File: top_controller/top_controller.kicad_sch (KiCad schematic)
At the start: 119 parts, among them J1 OUT1, J10 USB_C_Receptacle_USB2.0, J11 SWD, J12 UART, J13 BOOT0, J14 BOOT1, J2 OUT2, J3 OUT3, J4 OUT4, J5 OUT5, J6 OUT6, J7 OUT7, J8 OUT8, J9 PIN, SW1 RESET, U1 STM32F103C8Tx, U2 LT3045xMSE, U3 AD5754BREZ, U4 AD5754BREZ, U5 REF192, U6 EPM78V2, U7 REF192, Y1 8MHz

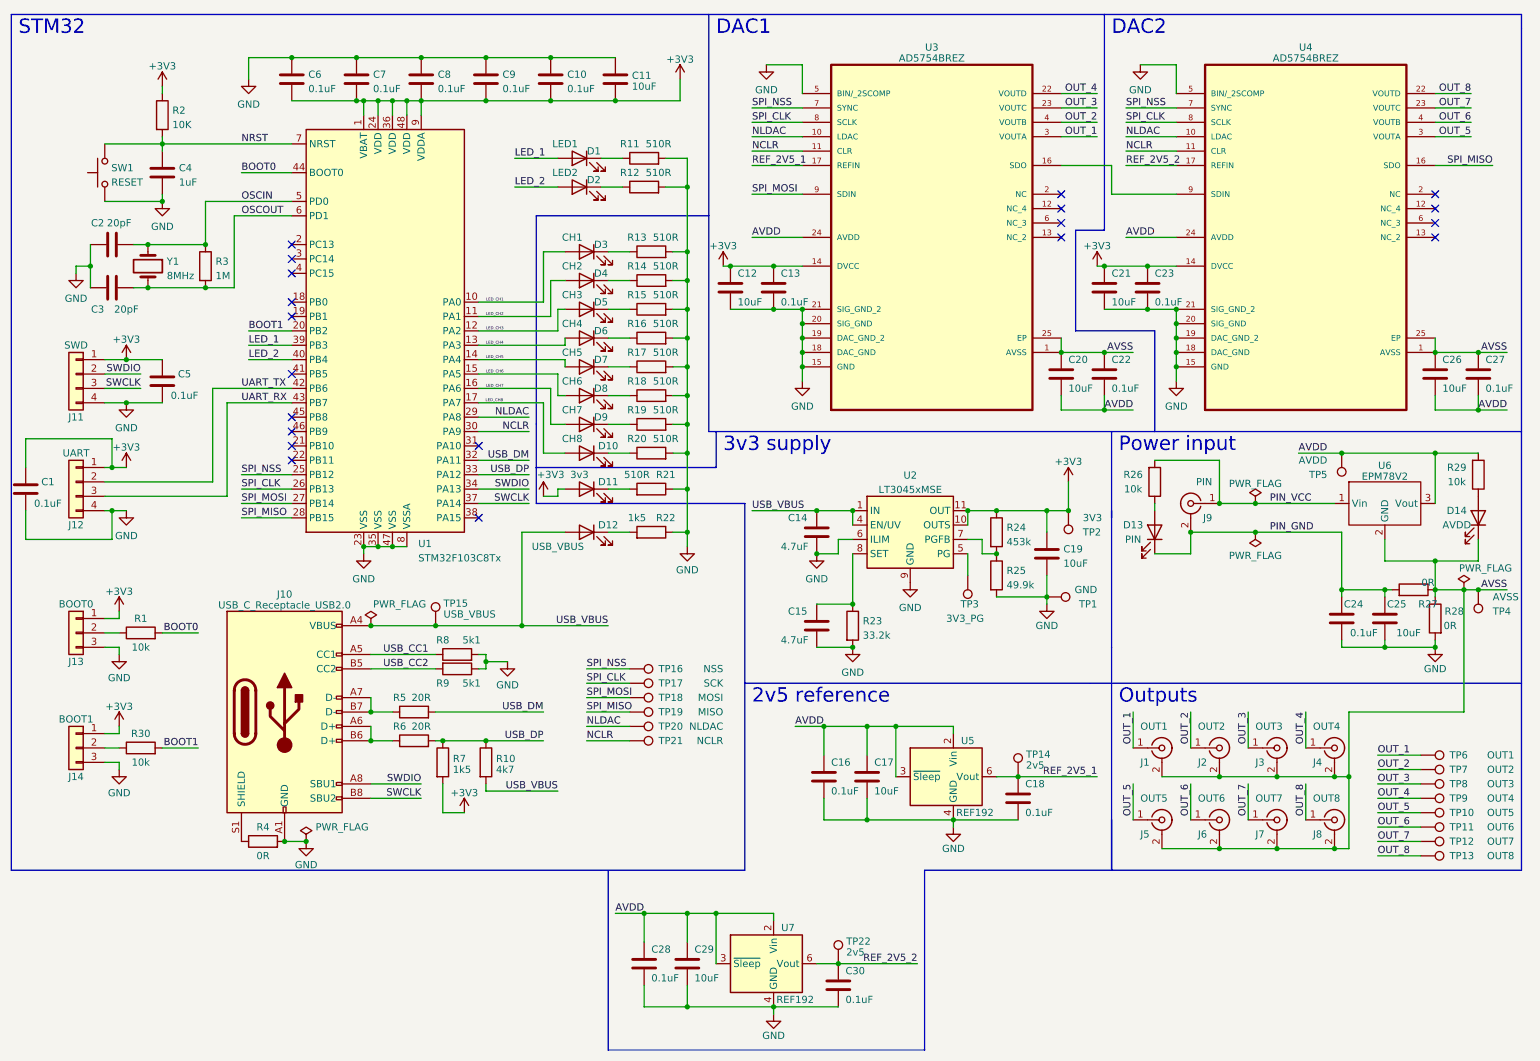
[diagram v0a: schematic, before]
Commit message: GNDA and VDDA redone properly, slightly changed component placement in the schematic
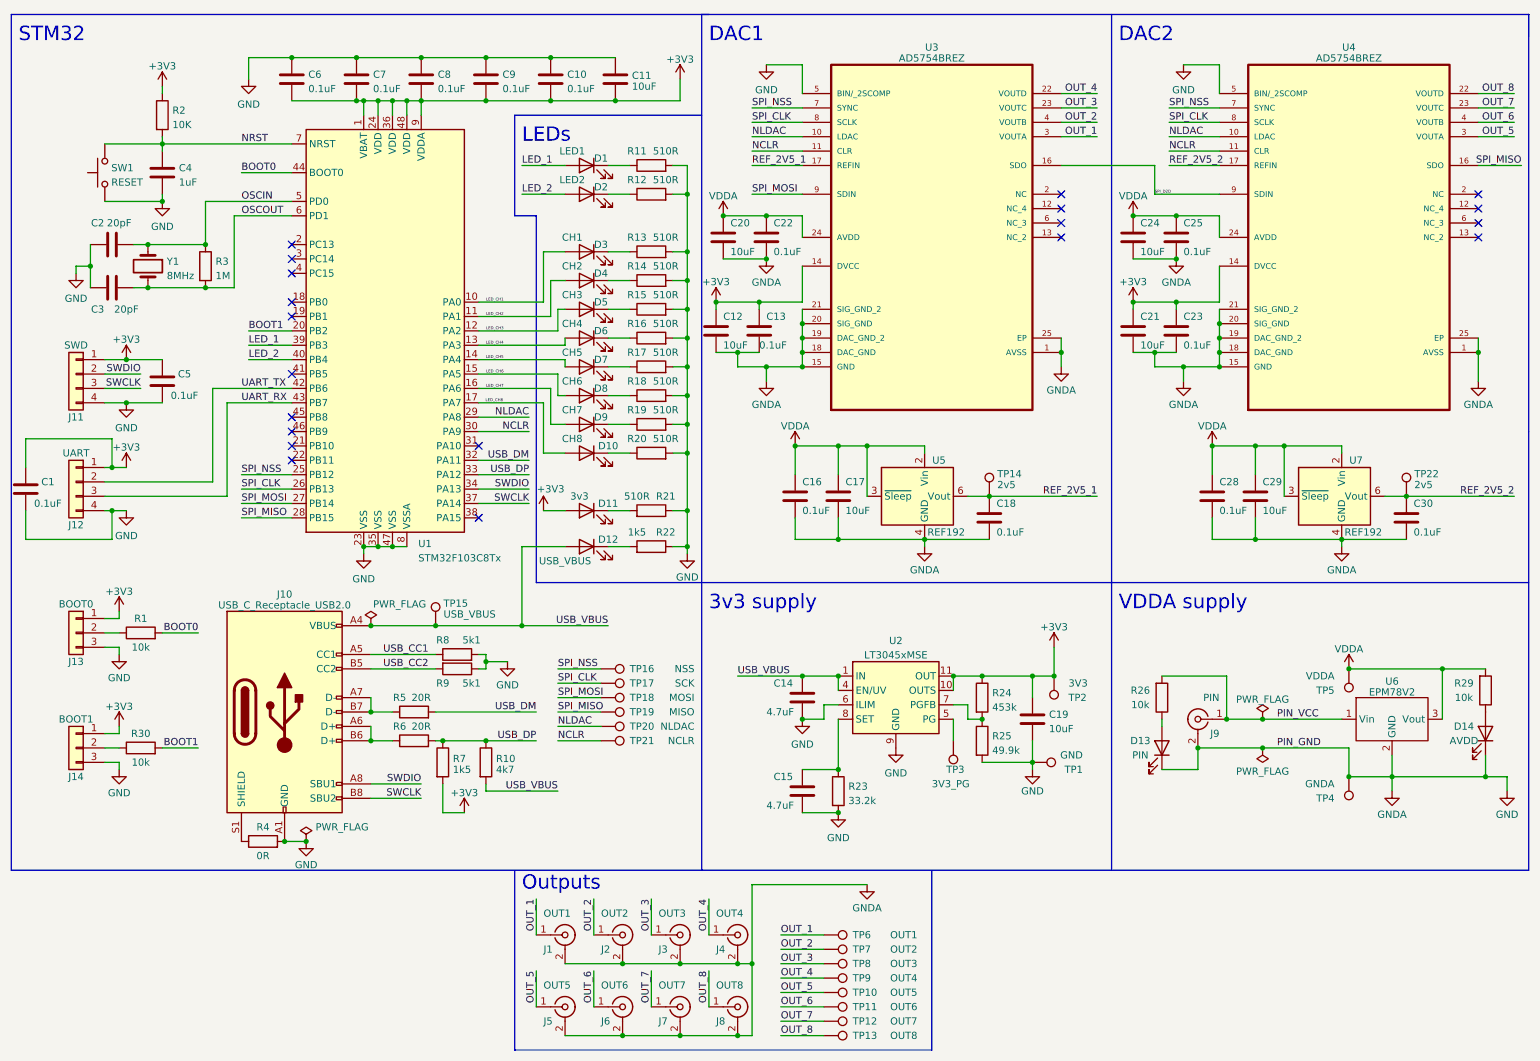
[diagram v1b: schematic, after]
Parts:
- removed C26: 10uF, Capacitor_SMD:C_1206_3216Metric, symbol Device:C
- removed C27: 0.1uF, Capacitor_SMD:C_0603_1608Metric, symbol Device:C
- removed R27, R28: 0R, Resistor_SMD:R_0603_1608Metric, symbol Device:R
- C24: value 0.1uF -> 10uF; footprint Capacitor_SMD:C_0603_1608Metric -> Capacitor_SMD:C_1206_3216Metric
- C25: value 10uF -> 0.1uF; footprint Capacitor_SMD:C_1206_3216Metric -> Capacitor_SMD:C_0603_1608Metric
- TP4: value AVSS -> GNDA
- TP5: value AVDD -> VDDA
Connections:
- net GND: now also C20.2, C22.2, D13.1 (K), D14.1 (K), J1.2 (Ext), J2.2 (Ext), J3.2 (Ext), J4.2 (Ext), J5.2 (Ext), J6.2 (Ext), J7.2 (Ext), J8.2 (Ext), J9.2 (Ext), TP4.1, U3.1 (AVSS), U3.25 (EP), U4.1 (AVSS), U4.25 (EP), U6.2 (GND)
- net SPI_D2D: now reaches U3.16 (SDO), U4.9 (SDIN)
- net AVDD renamed VDDA
- net VDDA: now also C20.1, C22.1, C24.1, C25.1; no longer C20.2, C22.2
- removed net AVSS: C20.1, C22.1, D14.1 (K), J1.2 (Ext), J2.2 (Ext), J3.2 (Ext), J4.2 (Ext), J5.2 (Ext), J6.2 (Ext), J7.2 (Ext), J8.2 (Ext), TP4.1, U3.1 (AVSS), U3.25 (EP), U4.1 (AVSS), U4.25 (EP), U6.2 (GND)
- removed net PIN_GND: C24.1, C25.1, D13.1 (K), J9.2 (Ext)
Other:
- note added: "LEDs"
- note added: "VDDA supply"
- note removed: "2v5 reference"
- note removed: "Power input"
- moved on the sheet: C12, C13, C14, C15, C16, C17, C18, C19, C21, C23, C28, C29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

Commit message: Restructured schematic again - LEDs moved to better locations
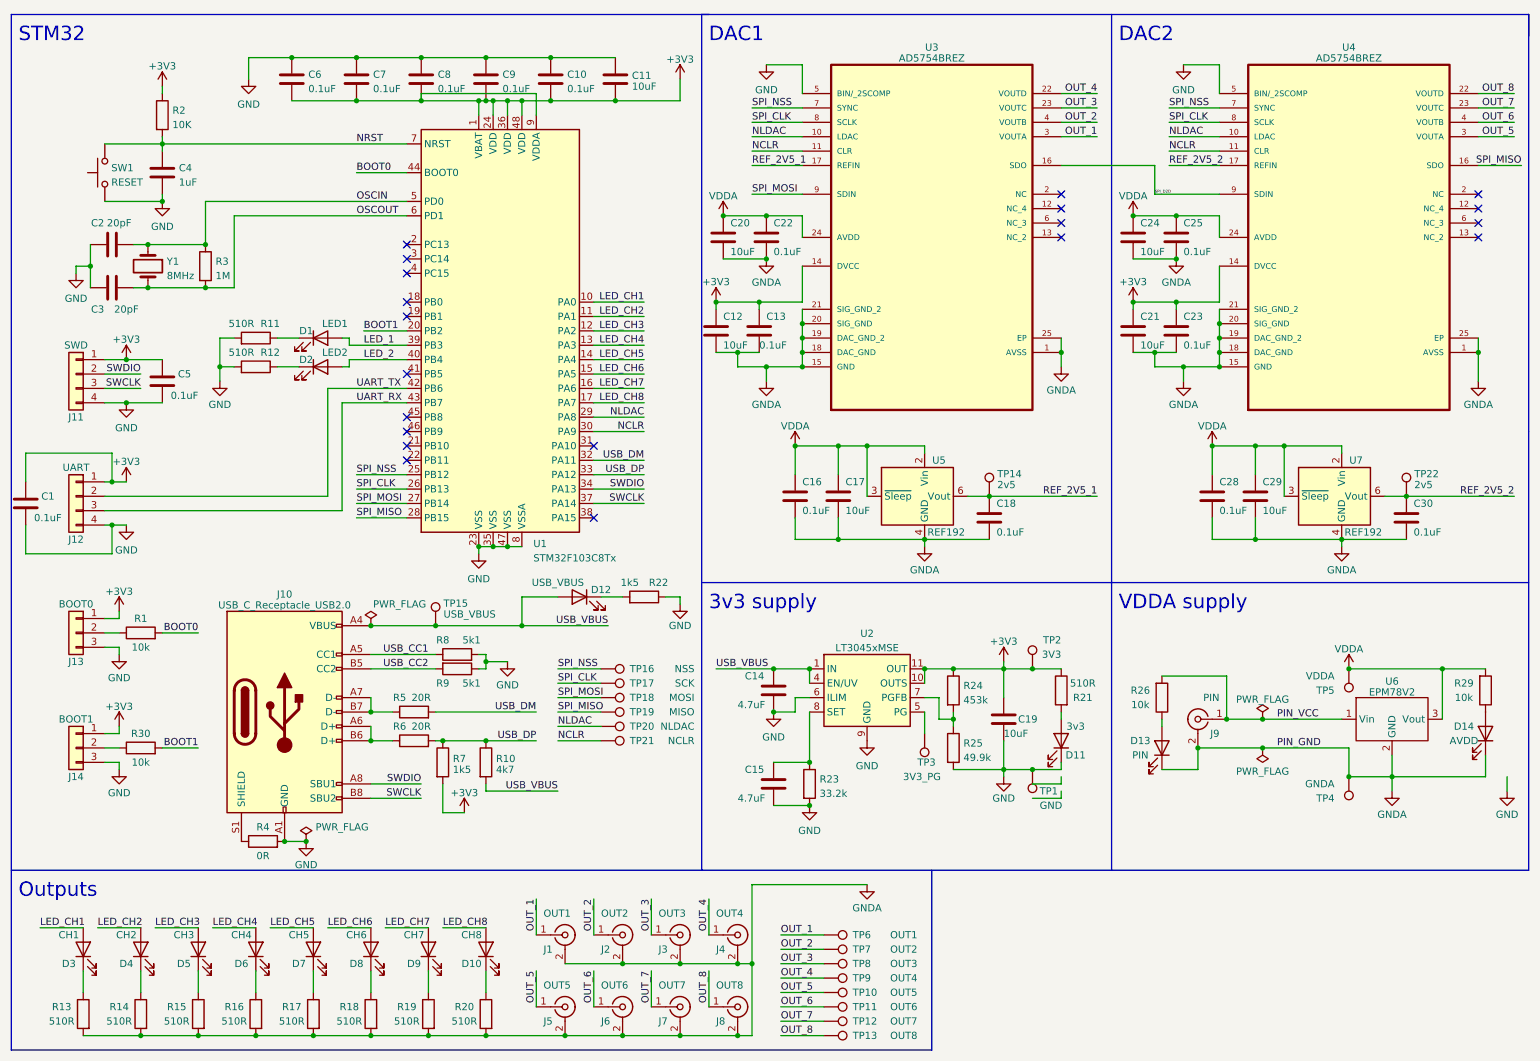
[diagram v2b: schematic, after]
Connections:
- net +3V3: now also R21.1; no longer D11.2 (A)
- net GND: now also D11.1 (K); no longer C12.2, C13.2, C16.2, C17.2, C18.2, C20.2, C21.2, C22.2, C23.2, C24.2, C25.2, C28.2, C29.2, C30.2, D13.1 (K), D14.1 (K), J1.2 (Ext), J2.2 (Ext), J3.2 (Ext), J4.2 (Ext), J5.2 (Ext), J6.2 (Ext), J7.2 (Ext), J8.2 (Ext), J9.2 (Ext), R13.2, R14.2, R15.2, R16.2, R17.2, R18.2, R19.2, R20.2, R21.1, TP4.1, U3.1 (AVSS), U3.15 (GND), U3.18 (DAC_GND), U3.19 (DAC_GND_2), U3.20 (SIG_GND), U3.21 (SIG_GND_2), U3.25 (EP), U4.1 (AVSS), U4.15 (GND), U4.18 (DAC_GND), U4.19 (DAC_GND_2), U4.20 (SIG_GND), U4.21 (SIG_GND_2), U4.25 (EP), U5.4 (GND), U6.2 (GND), U7.4 (GND)
- net at R21.2: now also D11.2 (A); no longer D11.1 (K)
- new net GNDA: C12.2, C13.2, C16.2, C17.2, C18.2, C20.2, C21.2, C22.2, C23.2, C24.2, C25.2, C28.2, C29.2, C30.2, D13.1 (K), D14.1 (K), J1.2 (Ext), J2.2 (Ext), J3.2 (Ext), J4.2 (Ext), J5.2 (Ext), J6.2 (Ext), J7.2 (Ext), J8.2 (Ext), J9.2 (Ext), R13.2, R14.2, R15.2, R16.2, R17.2, R18.2, R19.2, R20.2, TP4.1, U3.1 (AVSS), U3.15 (GND), U3.18 (DAC_GND), U3.19 (DAC_GND_2), U3.20 (SIG_GND), U3.21 (SIG_GND_2), U3.25 (EP), U4.1 (AVSS), U4.15 (GND), U4.18 (DAC_GND), U4.19 (DAC_GND_2), U4.20 (SIG_GND), U4.21 (SIG_GND_2), U4.25 (EP), U5.4 (GND), U6.2 (GND), U7.4 (GND)
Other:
- note removed: "LEDs"
- moved on the sheet: C1, C14, C15, C19, D1, D12, D2, J12, R11, R12, R22, R23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

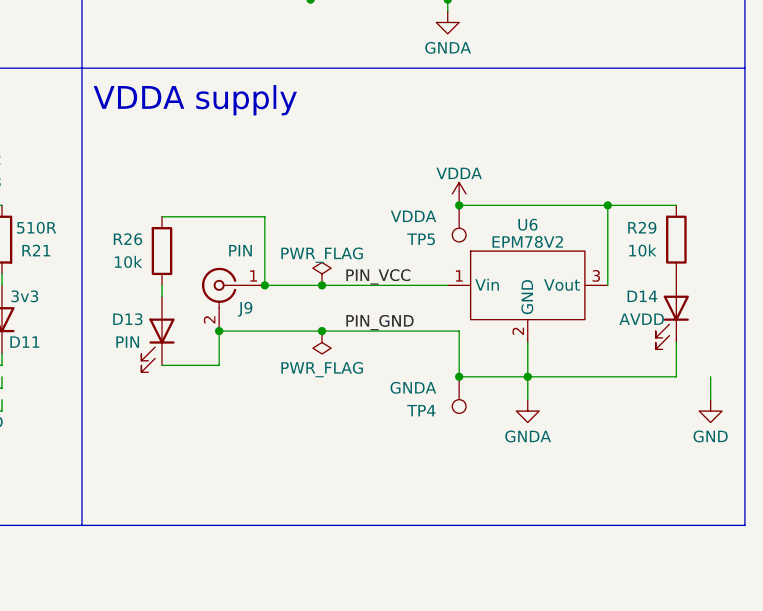
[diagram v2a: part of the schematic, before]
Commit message: Added capacitors around DC-DC regulator
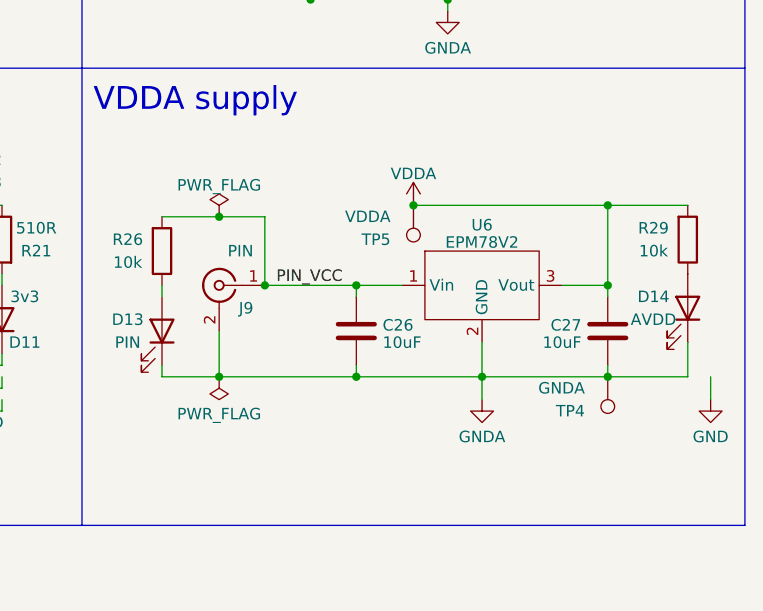
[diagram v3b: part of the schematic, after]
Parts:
- added C26, C27: 10uF, Capacitor_SMD:C_1206_3216Metric, symbol Device:C
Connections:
- net GNDA: now also C26.2, C27.2
- net PIN_VCC: now also C26.1
- net VDDA: now also C27.1
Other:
- moved on the sheet: D14, R29, TP4, TP5, U6
